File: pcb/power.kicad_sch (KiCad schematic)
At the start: 1 part, among them J3 Power

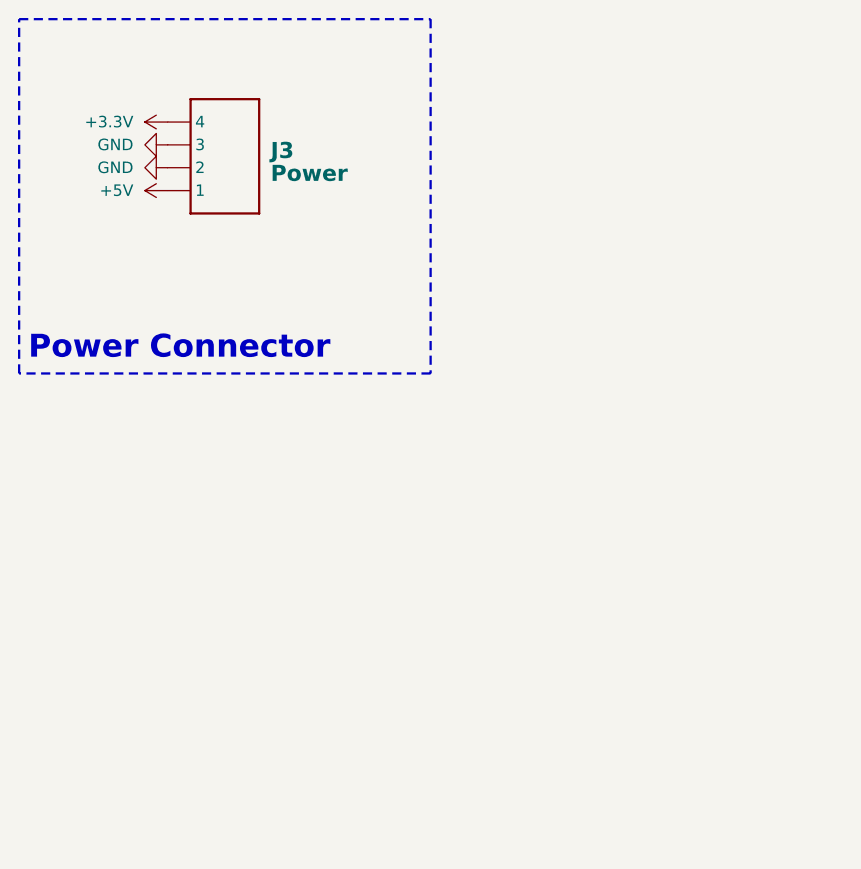
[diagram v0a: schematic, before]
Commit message: Updated license and implemented RP2040
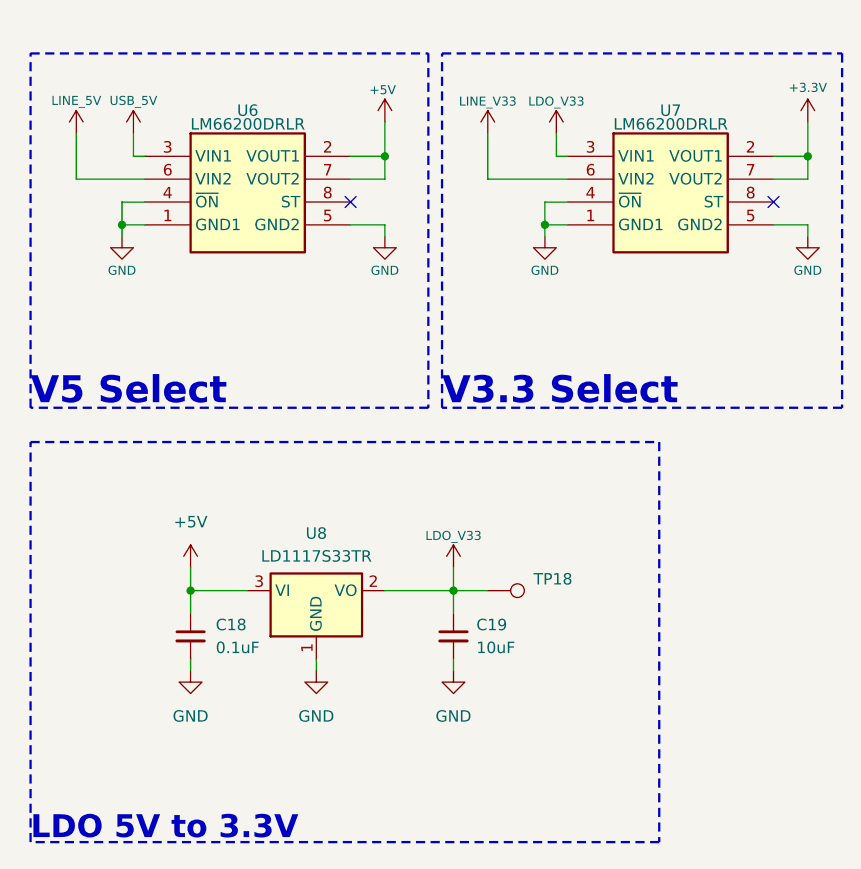
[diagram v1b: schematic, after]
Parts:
- removed J3: Power, Connector_JST:JST_SH_SM04B-SRSS-TB_1x04-1MP_P1.00mm_Horizontal, symbol CRGM Connector:JST-SH-4
- added C18: 0.1uF, Capacitor_SMD:C_0603_1608Metric, symbol Device:C_Small
- added C19: 10uF, Capacitor_SMD:C_0603_1608Metric, symbol Device:C_Small
- added TP18: ~, CRGM Mechanical:TestPoint_Pad_D1.0mm, symbol Connector:TestPoint
- added U6, U7: LM66200DRLR, CRGM Power:SOTFL50P160X60-8N, symbol CRGM Power:LM66200DRLR
- added U8: LD1117S33TR, CRGM Power:SOT230P700X180-4N, symbol Regulator_Linear:LD1117S33TR_SOT223
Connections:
- net +3.3V: now also U7.2 (VOUT1), U7.7 (VOUT2)
- net +5V: now also C18.1, U6.2 (VOUT1), U6.7 (VOUT2), U8.3 (VI)
- net GND: now also C18.2, C19.2, U6.1 (GND1), U6.4 (~{ON}), U6.5 (GND2), U7.1 (GND1), U7.4 (~{ON}), U7.5 (GND2), U8.1 (GND)
- new net LDO_V33: C19.1, TP18.1, U7.3 (VIN1), U8.2 (VO)
- new net LINE_5V: U6.6 (VIN2)
- new net LINE_V33: U7.6 (VIN2)
- new net USB_5V: U6.3 (VIN1)
- no-connect marks 0 -> 2
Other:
- note added: "LDO 5V to 3.3V"
- note added: "V3.3 Select"
- note added: "V5 Select"
- note removed: "Power Connector"
